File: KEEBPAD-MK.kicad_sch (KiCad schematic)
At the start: 19 parts, among them J2 USB_C_Receptacle_USB2.0, SW1 SW_SPST, SW2 SW_SPST, SW3 SW_SPST, SW4 SW_SPST, SW5 SW_SPST, SW6 SW_SPST, SW7 SW_SPST, SW8 SW_SPST

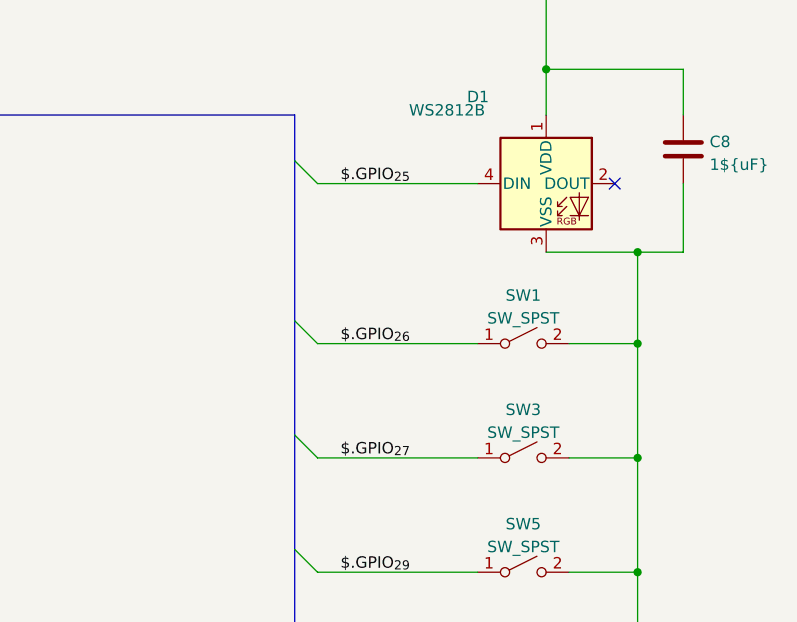
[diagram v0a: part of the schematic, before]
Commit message: Fixed SPI pin assignments to SPI0 only
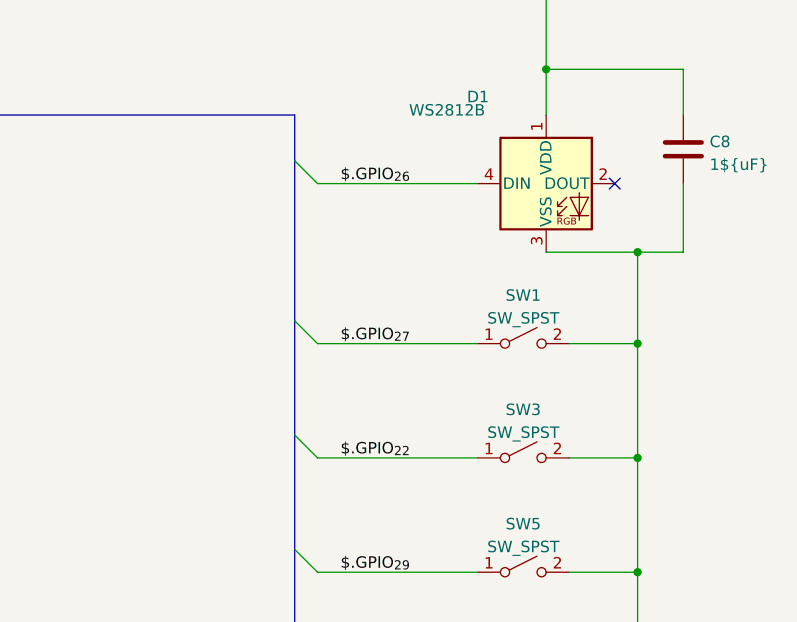
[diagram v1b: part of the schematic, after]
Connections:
- net $.GPIO_{25} is gone; now on net $.GPIO_{26}: D1.4 (DIN)
- net $.GPIO_{26}: no longer SW1.1 (A)
- net $.GPIO_{27}: now also SW1.1 (A); no longer SW3.1 (A)
- new net $.GPIO_{22}: SW3.1 (A)
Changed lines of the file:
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@@
     (effects (font (size 1.27 1.27)) (justify left bottom))
   )
-  (label "$.GPIO_{25}" (at 185.42 76.2 0)
+  (label "$.GPIO_{26}" (at 185.42 76.2 0)
     (effects (font (size 1.27 1.27)) (justify left bottom))
   )
@@
     (effects (font (size 1.27 1.27)) (justify left bottom))
   )
-  (label "$.GPIO_{26}" (at 185.42 93.98 0)
+  (label "$.GPIO_{22}" (at 185.42 106.68 0)
     (effects (font (size 1.27 1.27)) (justify left bottom))
   )
@@
     (effects (font (size 1.27 1.27)) (justify right bottom))
   )
-  (label "$.GPIO_{27}" (at 185.42 106.68 0)
+  (label "$.GPIO_{27}" (at 185.42 93.98 0)
     (effects (font (size 1.27 1.27)) (justify left bottom))
   )
